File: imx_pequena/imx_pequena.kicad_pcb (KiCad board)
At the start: 2 copper layers, 164 parts, among them J1 Conn_ARM_JTAG_SWD_10, J10 Conn_02x06_Top_Bottom, J11 Conn_02x06_Top_Bottom, J12 Conn_02x06_Top_Bottom, J2 Micro_SD_Card, J3 Conn_01x04, J4 USB_C_Receptacle, J5 USB_A, J6 Conn_02x06_Top_Bottom, J7 Conn_02x06_Top_Bottom, J8 Conn_02x06_Top_Bottom, J9 Conn_02x06_Top_Bottom, SW1 SW_SPST, SW2 SW_SPST, U1 MCIMX6Z0DVM09AB, U2 MT41K64M16TW-107:J_TR, U3 AP62250Z6, U4 AP62250Z6, X1 ASE-xxxMHz, Y2 Crystal

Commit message: lots of updates
Set design rules, fixed ERC, etc....
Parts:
- J10, J11, J12, J6, J7, J8, J9: footprint Connector_PinHeader_2.54mm:PinHeader_2x06_P2.54mm_Horizontal -> Connector_PinSocket_2.54mm:PinSocket_2x06_P2.54mm_Horizontal
- moved J6 129.7 mm to (151.9, 126.2)
- moved J4 114.5 mm to (125.2, 150.9)
- moved J11 104.5 mm to (113.0, 108.5)
- moved J8 17.6 mm to (113.0, 129.8), turned to 0 degrees
- moved H1 12.0 mm to (109.4, 78.0)
- moved J5 10.4 mm to (87.1, 45.1), turned to 180 degrees
- moved U3 8.19 mm to (112.7, 96.3)

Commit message: Layout updates
moved pmod connectors
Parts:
- moved J9 148.2 mm to (142.8, 137.0), turned to 180 degrees
- moved J10 126.8 mm to (142.8, 118.1), turned to 180 degrees
- moved J12 95.6 mm to (110.8, 86.6), turned to -90 degrees
- moved H4 92.8 mm to (152.0, 146.3)
- moved J5 92.6 mm to (102.0, 136.4), turned to 0 degrees
- moved J7 77.3 mm to (93.5, 85.0)
- moved H1 72.8 mm to (84.2, 146.3)
- moved H2 39.0 mm to (84.2, 77.5)
- moved H3 34.3 mm to (152.0, 77.5)
- moved J6 30.0 mm to (142.8, 97.6), turned to 180 degrees
- moved U2 20.9 mm to (120.8, 91.2)
- moved J8 20.3 mm to (93.5, 124.4)
- moved J11 19.8 mm to (93.5, 105.5)
- moved U1 17.8 mm to (120.8, 112.1)
- moved J4 7.85 mm to (121.1, 144.2)
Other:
- board outline added: 76.2 x 76.2 mm

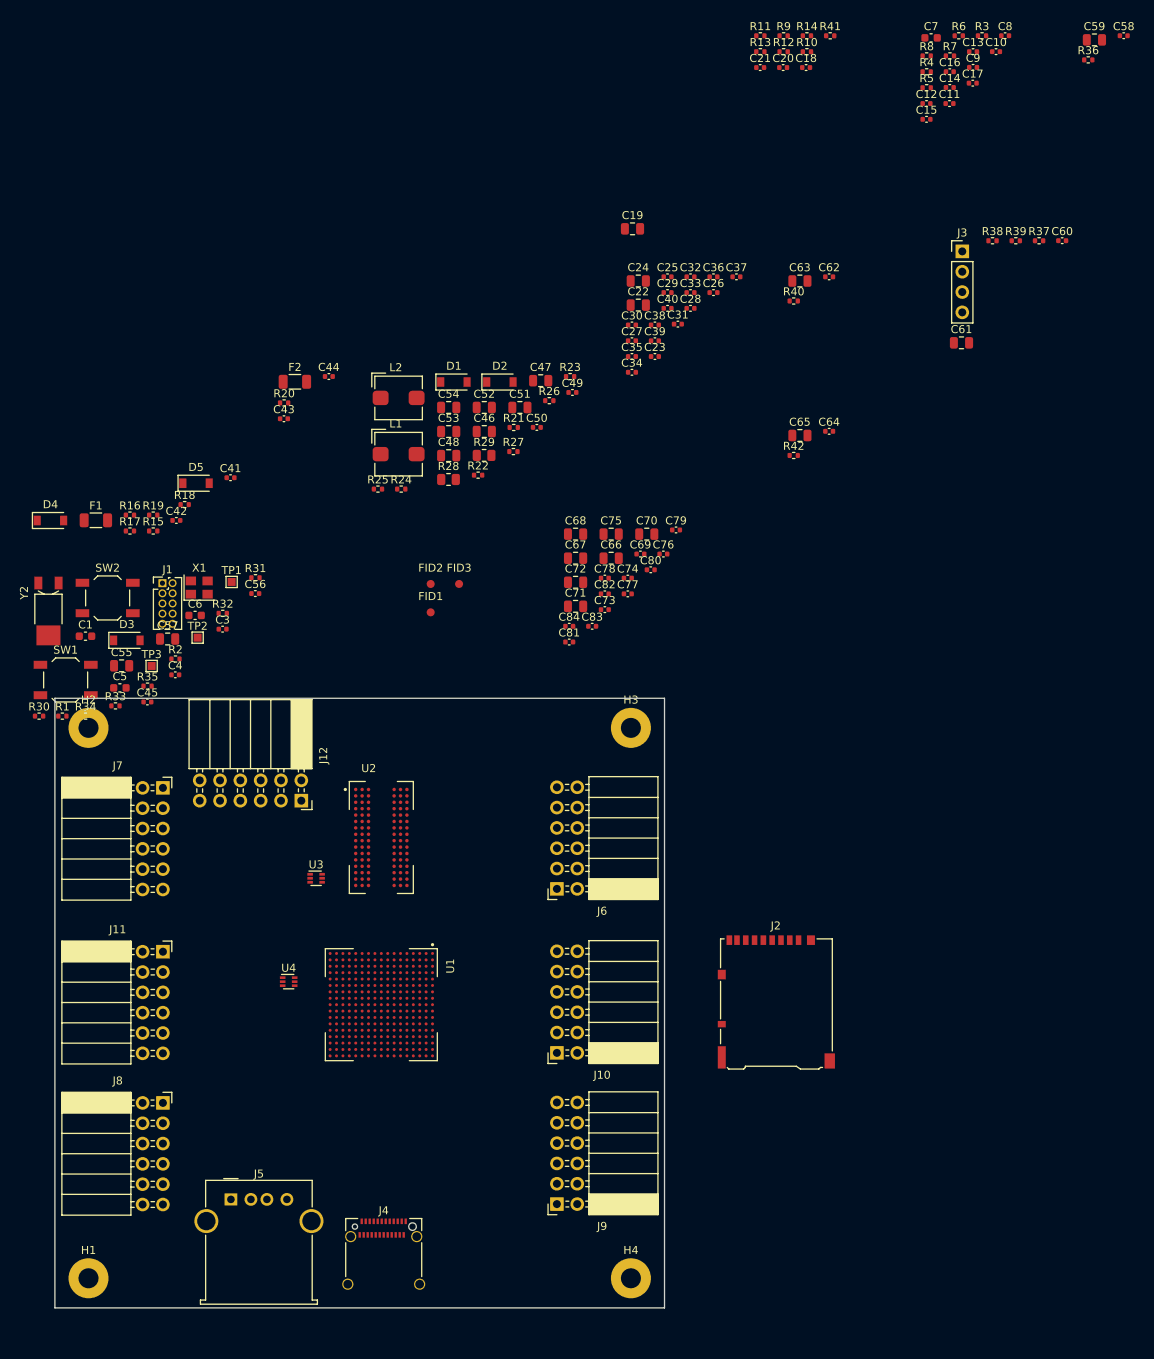
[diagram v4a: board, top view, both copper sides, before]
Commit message: fixed part alllocation
fixed socket to pin header issue
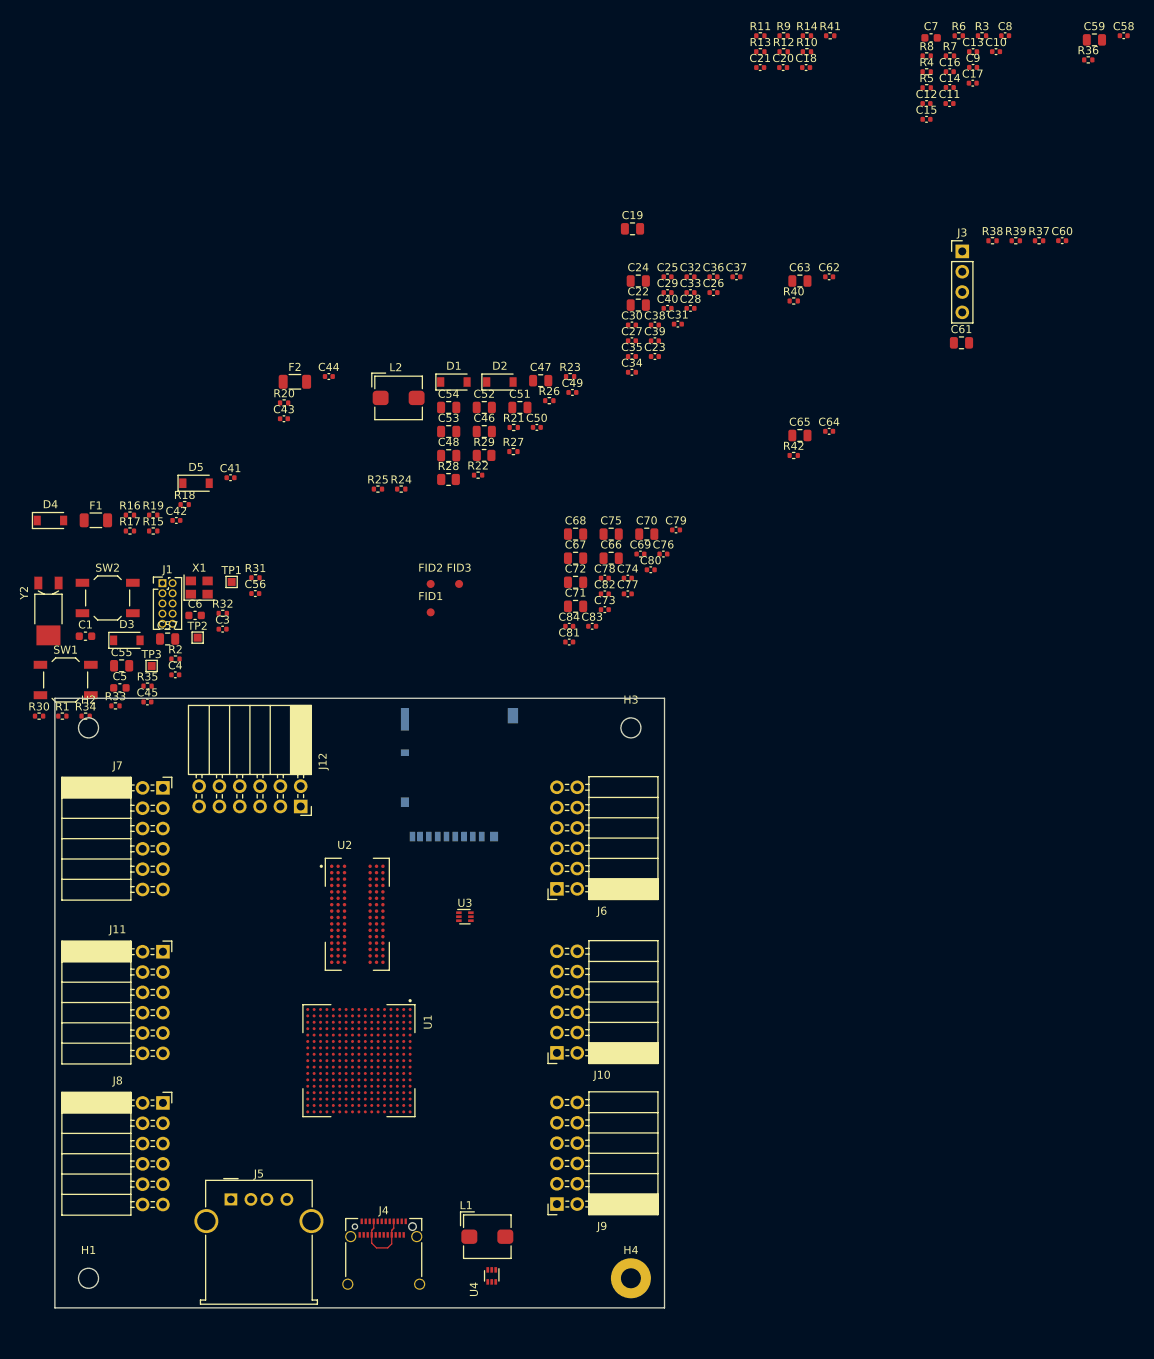
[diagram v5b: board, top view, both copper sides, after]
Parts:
- H1, H2, H3: footprint MountingHole:MountingHole_2.5mm_Pad -> MountingHole:MountingHole_2.5mm
- J2: moved to B.Cu
- moved L1 98.4 mm to (134.1, 141.1)
- moved J2 48.7 mm to (130.6, 83.4)
- moved U4 44.7 mm to (134.6, 146.0), turned to -90 degrees
- moved U3 19.2 mm to (131.2, 101.1)
- moved U2 10.1 mm to (117.8, 100.8)
- moved U1 7.54 mm to (118.0, 119.1)
- moved J12 0.73 mm to (110.7, 87.3)
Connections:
- J10 pad 1: /imx_mpu/pinouts/UART1_CTS -> /imx_mpu/UART1_CTS
- J10 pad 2: /imx_mpu/pinouts/UART1_TX -> /imx_mpu/UART1_TX
- J10 pad 3: /imx_mpu/pinouts/UART1_RX -> /imx_mpu/UART1_RX
- J10 pad 4: /imx_mpu/pinouts/UART1_RTS -> /imx_mpu/UART1_RTS
- J11 pad 1: unconnected-(J11-Pad1) -> /imx_mpu/UART3_TX
- J11 pad 2: unconnected-(J11-Pad2) -> /imx_mpu/UART3_RX
- J11 pad 3: /imx_mpu/pinouts/I2C2_SCL -> /imx_mpu/I2C2_SCL
- J11 pad 4: /imx_mpu/pinouts/I2C2_SDA -> /imx_mpu/I2C2_SDA
- J7 pad 1: /imx_mpu/pinouts/UART2_CTS -> /imx_mpu/UART2_CTS
- J7 pad 2: /imx_mpu/pinouts/UART2_TX -> /imx_mpu/UART2_TX
- J7 pad 3: /imx_mpu/pinouts/UART2_RX -> /imx_mpu/UART2_RX
- J7 pad 4: /imx_mpu/pinouts/UART2_RTS -> /imx_mpu/UART2_RTS
- J9 pad 3: /imx_mpu/pinouts/I2C1_SCL -> /imx_mpu/I2C1_SCL
- J9 pad 4: /imx_mpu/pinouts/I2C1_SDA -> /imx_mpu/I2C1_SDA
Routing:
- net Net-(F2-Pad1): track 0.00 -> 8.70 mm
- added copper zone on In1.Cu, net GND
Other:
- copper layers 2 -> 6
